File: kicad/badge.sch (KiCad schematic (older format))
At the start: 12 parts, among them SW1 SPST

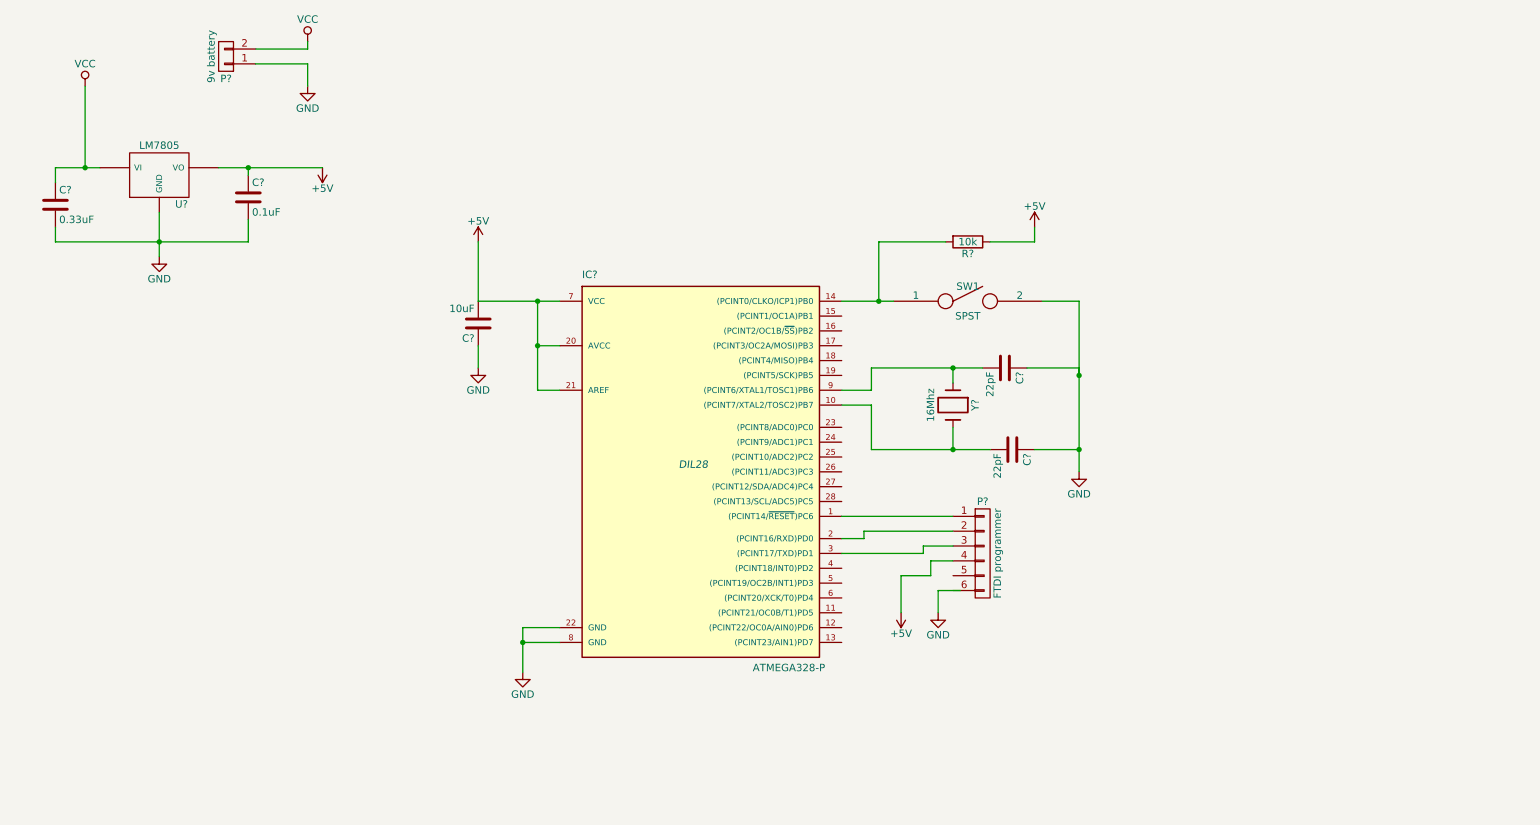
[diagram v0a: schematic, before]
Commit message: use wire labels to organize schematic
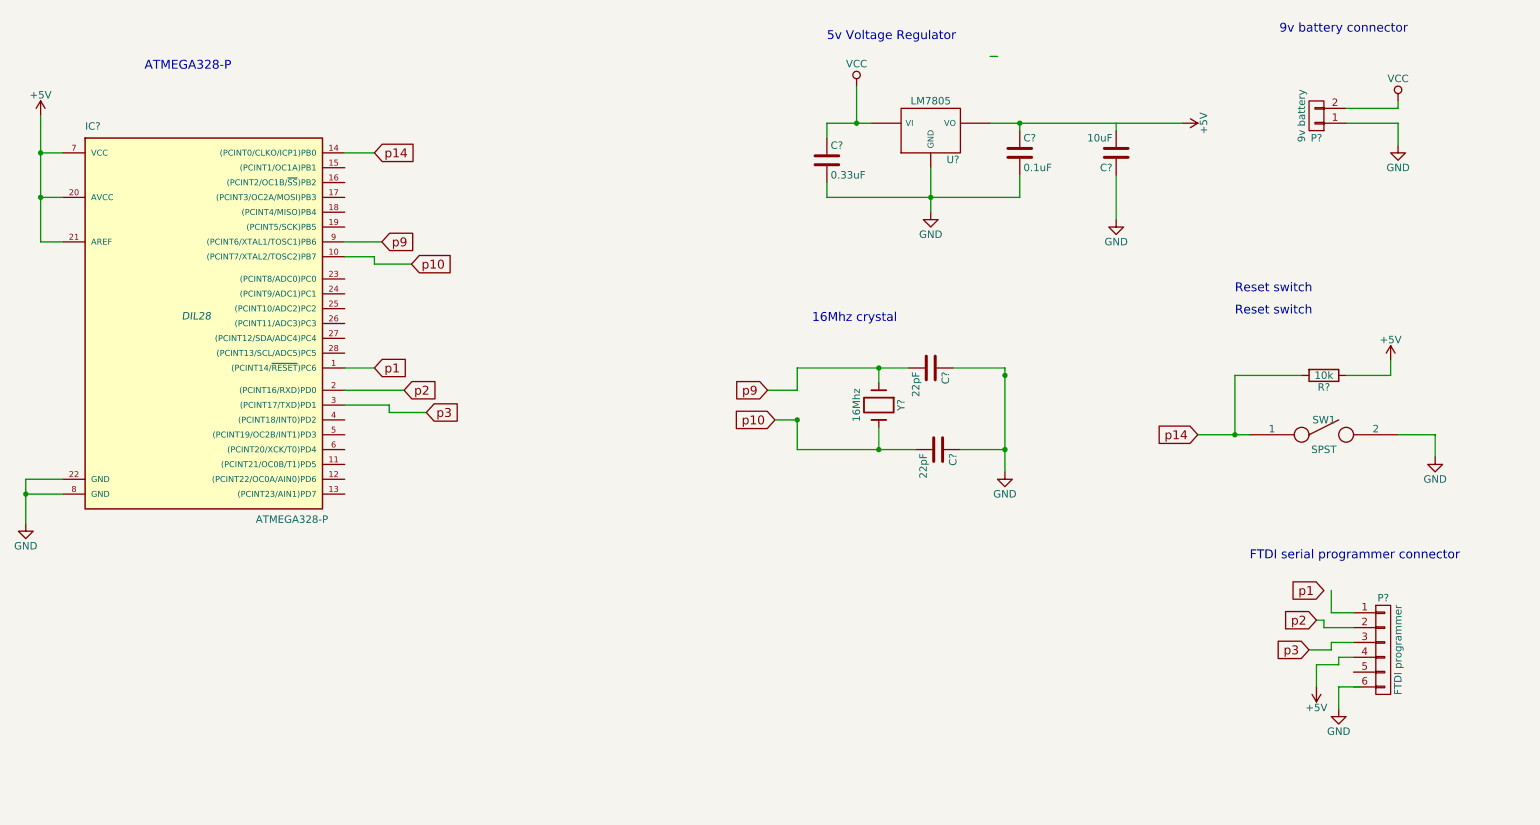
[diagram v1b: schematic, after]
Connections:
- net labels added: p1, p10, p14, p2, p3, p9
- wire segments 53 -> 65
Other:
- note added: "16Mhz crystal"
- note added: "5v Voltage Regulator"
- note added: "9v battery connector"
- note added: "ATMEGA328-P"
- note added: "FTDI serial programmer connector"
- note added: "Reset switch"
- moved on the sheet: C?, IC?, P?, R?, SW1, U?, Y?

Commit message: display connector
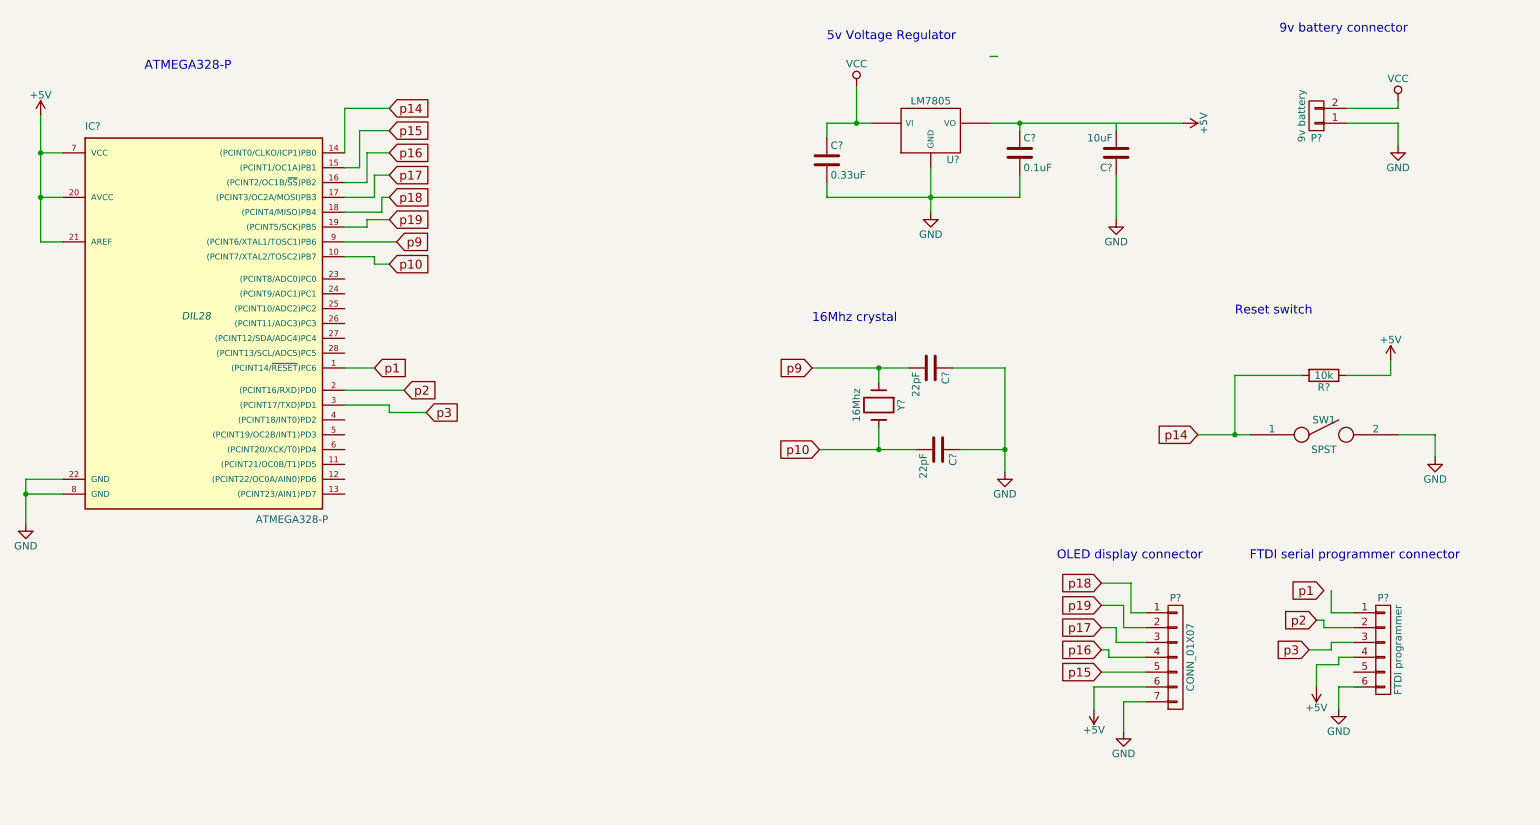
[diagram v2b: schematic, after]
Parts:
- added P?: CONN_01X07, symbol CONN_01X07
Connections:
- net labels added: p15, p16, p17, p18, p19
- wire segments 65 -> 94
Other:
- note added: "OLED display connector"
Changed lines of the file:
@@
 	1    0    0    -1
 $EndComp
-Text GLabel 3450 1650 2    60   Input ~ 0
+Text GLabel 3550 1350 2    60   Input ~ 0
 p14
 Text GLabel 9000 3550 0    60   Input ~ 0
 p14
-Text GLabel 3500 2250 2    60   Input ~ 0
+Text GLabel 3600 2250 2    60   Input ~ 0
 p9
-Text GLabel 3700 2400 2    60   Input ~ 0
+Text GLabel 3550 2400 2    60   Input ~ 0
 p10
-Text GLabel 6100 3250 0    60   Input ~ 0
+Text GLabel 6400 3100 0    60   Input ~ 0
 p9
-Text GLabel 6150 3450 0    60   Input ~ 0
+Text GLabel 6450 3650 0    60   Input ~ 0
 p10
 Text GLabel 3450 3100 2    60   Input ~ 0
@@
 $EndComp
 Wire Wire Line
-	6300 3100 7050 3100
-Wire Wire Line
 	6850 3200 6850 3100
 Wire Wire Line
 	6850 3500 6850 3650
-Wire Wire Line
-	6300 3650 7100 3650
 Wire Wire Line
 	7350 3100 7700 3100
@@
 	6700 1200 6700 1450
 Connection ~ 6700 1450
-Wire Wire Line
-	6100 3250 6300 3250
-Wire Wire Line
-	6300 3250 6300 3100
 Connection ~ 6850 3100
 Connection ~ 6850 3650
@@
 Wire Wire Line
 	10350 3550 10600 3550
-Connection ~ 7700 3150
 Wire Wire Line
 	10000 1350 10350 1350
@@
 	10600 3550 10600 3700
 Wire Wire Line
-	3250 1650 3450 1650
-Wire Wire Line
-	3250 2250 3500 2250
+	3250 2250 3600 2250
 Wire Wire Line
 	3250 2350 3450 2350
@@
 	3450 2350 3450 2400
 Wire Wire Line
-	3450 2400 3700 2400
-Wire Wire Line
-	6150 3450 6300 3450
-Connection ~ 6300 3450
-Wire Wire Line
-	6300 3450 6300 3650
-Wire Wire Line
 	3250 3100 3450 3100
 Wire Wire Line
@@
 	1200 2250 1350 2250
 Wire Wire Line
-	1350 1950 1200 1950
+	1200 1950 1350 1950
 Connection ~ 1200 1650
 Connection ~ 1200 1950
@@
 Text Notes 6400 2800 0    60   ~ 0
 16Mhz crystal
-Text Notes 9250 2600 0    60   ~ 0
-Reset switch
 Text Notes 9350 4400 0    60   ~ 0
 FTDI serial programmer connector
@@
 Text Notes 9250 2750 0    60   ~ 0
 Reset switch
+Wire Wire Line
+	6400 3100 7050 3100
+Wire Wire Line
+	6450 3650 7100 3650
+$Comp
+L GND #PWR?
+U 1 1 58E46BE0
+P 8500 5550
+F 0 "#PWR?" H 8500 5300 50  0001 C CNN
+F 1 "GND" H 8500 5400 50  0000 C CNN
+F 2 "" H 8500 5550 50  0000 C CNN
+F 3 "" H 8500 5550 50  0000 C CNN
+	1    8500 5550
+	1    0    0    -1
+$EndComp
+Wire Wire Line
+	8650 5350 8500 5350
+Wire Wire Line
+	8500 5350 8500 5550
+$Comp
+L +5V #PWR?
+U 1 1 58E46C64
+P 8300 5400
+F 0 "#PWR?" H 8300 5250 50  0001 C CNN
+F 1 "+5V" H 8300 5540 50  0000 C CNN
+F 2 "" H 8300 5400 50  0000 C CNN
+F 3 "" H 8300 5400 50  0000 C CNN
+	1    8300 5400
+	-1   0    0    1
+$EndComp
+Wire Wire Line
+	8650 5250 8300 5250
+Wire Wire Line
+	8300 5250 8300 5400
+Text GLabel 8350 4700 0    60   Input ~ 0
+p19
+Text GLabel 8350 4850 0    60   Input ~ 0
+p17
+Text GLabel 8350 5000 0    60   Input ~ 0
+p16
+Text GLabel 8350 5150 0    60   Input ~ 0
+p15
+Wire Wire Line
+	8350 5150 8650 5150
+Wire Wire Line
+	8350 5000 8400 5000
+Wire Wire Line
+	8400 5000 8400 5050
+Wire Wire Line
+	8400 5050 8650 5050
+Wire Wire Line
+	8350 4850 8450 4850
+Wire Wire Line
+	8450 4850 8450 4950
+Wire Wire Line
+	8450 4950 8650 4950
+Wire Wire Line
+	8350 4700 8500 4700
+Wire Wire Line
+	8500 4700 8500 4850
+Wire Wire Line
+	8500 4850 8650 4850
+$Comp
+L CONN_01X07 P?
+U 1 1 58E46FAC
+P 8850 5050
+F 0 "P?" H 8850 5450 50  0000 C CNN
+F 1 "CONN_01X07" V 8950 5050 50  0000 C CNN
+F 2 "" H 8850 5050 50  0000 C CNN
+F 3 "" H 8850 5050 50  0000 C CNN
+	1    8850 5050
+	1    0    0    -1
+$EndComp
+Text GLabel 8350 4550 0    60   Input ~ 0
+p18
+Wire Wire Line
+	8350 4550 8550 4550
+Wire Wire Line
+	8550 4550 8550 4750
+Wire Wire Line
+	8550 4750 8650 4750
+Text Notes 8050 4400 0    60   ~ 0
+OLED display connector
+Text GLabel 3550 1500 2    60   Input ~ 0
+p15
+Text GLabel 3550 1650 2    60   Input ~ 0
+p16
+Text GLabel 3550 1800 2    60   Input ~ 0
+p17
+Text GLabel 3550 1950 2    60   Input ~ 0
+p18
+Text GLabel 3550 2100 2    60   Input ~ 0
+p19
+Wire Wire Line
+	3250 2150 3400 2150
+Wire Wire Line
+	3400 2150 3400 2100
+Wire Wire Line
+	3400 2100 3550 2100
+Wire Wire Line
+	3250 2050 3500 2050
+Wire Wire Line
+	3500 2050 3500 1950
+Wire Wire Line
+	3500 1950 3550 1950
+Wire Wire Line
+	3250 1950 3450 1950
+Wire Wire Line
+	3450 1950 3450 1800
+Wire Wire Line
+	3450 1800 3550 1800
+Wire Wire Line
+	3250 1850 3400 1850
+Wire Wire Line
+	3400 1850 3400 1650
+Wire Wire Line
+	3400 1650 3550 1650
+Wire Wire Line
+	3250 1750 3350 1750
+Wire Wire Line
+	3350 1750 3350 1500
+Wire Wire Line
+	3350 1500 3550 1500
+Wire Wire Line
+	3250 1650 3250 1350
+Wire Wire Line
+	3250 1350 3550 1350
+Wire Wire Line
+	3450 2400 3550 2400
 $EndSCHEMATC

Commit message: netlist
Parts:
- gave numbers to parts that had none: 12
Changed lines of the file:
@@
 $EndDescr
 $Comp
-L R R?
+L R R1
 U 1 1 58E15AC1
 P 9850 3150
-F 0 "R?" V 9930 3150 50  0000 C CNN
+F 0 "R1" V 9930 3150 50  0000 C CNN
 F 1 "10k" V 9850 3150 50  0000 C CNN
 F 2 "" V 9780 3150 50  0000 C CNN
@@
 $EndComp
 $Comp
-L C C?
+L C C2
 U 1 1 58E15B8A
 P 7200 3100
-F 0 "C?" H 7225 3200 50  0000 L CNN
+F 0 "C2" H 7225 3200 50  0000 L CNN
 F 1 "22pF" H 7225 3000 50  0000 L CNN
 F 2 "" H 7238 2950 50  0000 C CNN
@@
 $EndComp
 $Comp
-L GND #PWR04
+L GND #PWR01
 U 1 1 58E16135
 P 7700 3800
-F 0 "#PWR04" H 7700 3550 50  0001 C CNN
+F 0 "#PWR01" H 7700 3550 50  0001 C CNN
 F 1 "GND" H 7700 3650 50  0000 C CNN
 F 2 "" H 7700 3800 50  0000 C CNN
@@
 $EndComp
 $Comp
-L C C?
+L C C5
 U 1 1 58E164D8
 P 8450 1650
-F 0 "C?" H 8475 1750 50  0000 L CNN
+F 0 "C5" H 8475 1750 50  0000 L CNN
 F 1 "10uF" H 8475 1550 50  0000 L CNN
 F 2 "" H 8488 1500 50  0000 C CNN
@@
 $EndComp
 $Comp
-L GND #PWR05
+L GND #PWR02
 U 1 1 58E16557
 P 8450 2100
-F 0 "#PWR05" H 8450 1850 50  0001 C CNN
+F 0 "#PWR02" H 8450 1850 50  0001 C CNN
 F 1 "GND" H 8450 1950 50  0000 C CNN
 F 2 "" H 8450 2100 50  0000 C CNN
@@
 $EndComp
 $Comp
-L LM7805 U?
+L LM7805 U1
 U 1 1 58E194B3
 P 7200 1500
-F 0 "U?" H 7350 1304 50  0000 C CNN
+F 0 "U1" H 7350 1304 50  0000 C CNN
 F 1 "LM7805" H 7200 1700 50  0000 C CNN
 F 2 "" H 7200 1500 50  0000 C CNN
@@
 $EndComp
 $Comp
-L GND #PWR?
+L GND #PWR03
 U 1 1 58E194EE
 P 7200 2050
-F 0 "#PWR?" H 7200 1800 50  0001 C CNN
+F 0 "#PWR03" H 7200 1800 50  0001 C CNN
 F 1 "GND" H 7200 1900 50  0000 C CNN
 F 2 "" H 7200 2050 50  0000 C CNN
@@
 $EndComp
 $Comp
-L C C?
+L C C4
 U 1 1 58E19514
 P 7800 1650
-F 0 "C?" H 7825 1750 50  0000 L CNN
+F 0 "C4" H 7825 1750 50  0000 L CNN
 F 1 "0.1uF" H 7825 1550 50  0000 L CNN
 F 2 "" H 7838 1500 50  0000 C CNN
@@
 $EndComp
 $Comp
-L C C?
+L C C1
 U 1 1 58E19563
 P 6500 1700
-F 0 "C?" H 6525 1800 50  0000 L CNN
+F 0 "C1" H 6525 1800 50  0000 L CNN
 F 1 "0.33uF" H 6525 1600 50  0000 L CNN
 F 2 "" H 6538 1550 50  0000 C CNN
@@
 $EndComp
 $Comp
-L +5V #PWR?
+L +5V #PWR04
 U 1 1 58E198B5
 P 10300 3050
-F 0 "#PWR?" H 10300 2900 50  0001 C CNN
+F 0 "#PWR04" H 10300 2900 50  0001 C CNN
 F 1 "+5V" H 10300 3190 50  0000 C CNN
 F 2 "" H 10300 3050 50  0000 C CNN
@@
 $EndComp
 $Comp
-L VCC #PWR?
+L VCC #PWR05
 U 1 1 58E19A0A
 P 6700 1200
-F 0 "#PWR?" H 6700 1050 50  0001 C CNN
+F 0 "#PWR05" H 6700 1050 50  0001 C CNN
 F 1 "VCC" H 6700 1350 50  0000 C CNN
 F 2 "" H 6700 1200 50  0000 C CNN
@@
 $EndComp
 $Comp
-L ATMEGA328-P IC?
+L ATMEGA328-P IC1
 U 1 1 58E19C48
 P 2250 2750
-F 0 "IC?" H 1500 4000 50  0000 L BNN
+F 0 "IC1" H 1500 4000 50  0000 L BNN
 F 1 "ATMEGA328-P" H 2650 1350 50  0000 L BNN
 F 2 "DIL28" H 2250 2750 50  0000 C CIN
@@
 $EndComp
 $Comp
-L CONN_01X02 P?
+L CONN_01X02 P2
 U 1 1 58E1B172
 P 9800 1400
-F 0 "P?" H 9800 1550 50  0000 C CNN
+F 0 "P2" H 9800 1550 50  0000 C CNN
 F 1 "9v battery " V 9900 1400 50  0000 C CNN
 F 2 "" H 9800 1400 50  0000 C CNN
@@
 $EndComp
 $Comp
-L VCC #PWR?
+L VCC #PWR06
 U 1 1 58E1B2A6
 P 10350 1300
-F 0 "#PWR?" H 10350 1150 50  0001 C CNN
+F 0 "#PWR06" H 10350 1150 50  0001 C CNN
 F 1 "VCC" H 10350 1450 50  0000 C CNN
 F 2 "" H 10350 1300 50  0000 C CNN
@@
 $EndComp
 $Comp
-L GND #PWR?
+L GND #PWR07
 U 1 1 58E1B2D2
 P 10350 1600
-F 0 "#PWR?" H 10350 1350 50  0001 C CNN
+F 0 "#PWR07" H 10350 1350 50  0001 C CNN
 F 1 "GND" H 10350 1450 50  0000 C CNN
 F 2 "" H 10350 1600 50  0000 C CNN
@@
 $EndComp
 $Comp
-L CONN_01X06 P?
+L CONN_01X06 P3
 U 1 1 58E1B8C9
 P 10250 5000
-F 0 "P?" H 10250 5350 50  0000 C CNN
+F 0 "P3" H 10250 5350 50  0000 C CNN
 F 1 "FTDI programmer" V 10350 5000 50  0000 C CNN
 F 2 "" H 10250 5000 50  0000 C CNN
@@
 $EndComp
 $Comp
-L GND #PWR?
+L GND #PWR08
 U 1 1 58E1B9A0
 P 9950 5400
-F 0 "#PWR?" H 9950 5150 50  0001 C CNN
+F 0 "#PWR08" H 9950 5150 50  0001 C CNN
 F 1 "GND" H 9950 5250 50  0000 C CNN
 F 2 "" H 9950 5400 50  0000 C CNN
@@
 $EndComp
 $Comp
-L +5V #PWR?
+L +5V #PWR09
 U 1 1 58E1BF97
 P 9800 5250
-F 0 "#PWR?" H 9800 5100 50  0001 C CNN
+F 0 "#PWR09" H 9800 5100 50  0001 C CNN
 F 1 "+5V" H 9800 5390 50  0000 C CNN
 F 2 "" H 9800 5250 50  0000 C CNN
@@
 $EndComp
 $Comp
-L Crystal Y?
+L Crystal Y1
 U 1 1 58E1C7EA
 P 6850 3350
-F 0 "Y?" H 6850 3500 50  0000 C CNN
+F 0 "Y1" H 6850 3500 50  0000 C CNN
 F 1 "16Mhz" H 6850 3200 50  0000 C CNN
 F 2 "" H 6850 3350 50  0000 C CNN
@@
 $EndComp
 $Comp
-L C C?
+L C C3
 U 1 1 58E1C898
 P 7250 3650
-F 0 "C?" H 7275 3750 50  0000 L CNN
+F 0 "C3" H 7275 3750 50  0000 L CNN
 F 1 "22pF" H 7275 3550 50  0000 L CNN
 F 2 "" H 7288 3500 50  0000 C CNN
@@
 $EndComp
 $Comp
-L GND #PWR?
+L GND #PWR010
 U 1 1 58E35C64
 P 10600 3700
-F 0 "#PWR?" H 10600 3450 50  0001 C CNN
+F 0 "#PWR010" H 10600 3450 50  0001 C CNN
 F 1 "GND" H 10600 3550 50  0000 C CNN
 F 2 "" H 10600 3700 50  0000 C CNN
@@
 p1
 $Comp
-L +5V #PWR?
+L +5V #PWR011
 U 1 1 58E36E45
 P 8900 1450
-F 0 "#PWR?" H 8900 1300 50  0001 C CNN
+F 0 "#PWR011" H 8900 1300 50  0001 C CNN
 F 1 "+5V" H 8900 1590 50  0000 C CNN
 F 2 "" H 8900 1450 50  0000 C CNN
@@
 $EndComp
 $Comp
-L GND #PWR01
+L GND #PWR012
 U 1 1 58E15A16
 P 1100 4150
-F 0 "#PWR01" H 1100 3900 50  0001 C CNN
+F 0 "#PWR012" H 1100 3900 50  0001 C CNN
 F 1 "GND" H 1100 4000 50  0000 C CNN
 F 2 "" H 1100 4150 50  0000 C CNN
@@
 	1200 1400 1200 2250
 $Comp
-L +5V #PWR?
+L +5V #PWR013
 U 1 1 58E37469
 P 1200 1400
-F 0 "#PWR?" H 1200 1250 50  0001 C CNN
+F 0 "#PWR013" H 1200 1250 50  0001 C CNN
 F 1 "+5V" H 1200 1540 50  0000 C CNN
 F 2 "" H 1200 1400 50  0000 C CNN
@@
 	6450 3650 7100 3650
 $Comp
-L GND #PWR?
+L GND #PWR014
 U 1 1 58E46BE0
 P 8500 5550
-F 0 "#PWR?" H 8500 5300 50  0001 C CNN
+F 0 "#PWR014" H 8500 5300 50  0001 C CNN
 F 1 "GND" H 8500 5400 50  0000 C CNN
 F 2 "" H 8500 5550 50  0000 C CNN
@@
 	8500 5350 8500 5550
 $Comp
-L +5V #PWR?
+L +5V #PWR015
 U 1 1 58E46C64
 P 8300 5400
-F 0 "#PWR?" H 8300 5250 50  0001 C CNN
+F 0 "#PWR015" H 8300 5250 50  0001 C CNN
 F 1 "+5V" H 8300 5540 50  0000 C CNN
 F 2 "" H 8300 5400 50  0000 C CNN
@@
 	8500 4850 8650 4850
 $Comp
-L CONN_01X07 P?
+L CONN_01X07 P1
 U 1 1 58E46FAC
 P 8850 5050
-F 0 "P?" H 8850 5450 50  0000 C CNN
+F 0 "P1" H 8850 5450 50  0000 C CNN
 F 1 "CONN_01X07" V 8950 5050 50  0000 C CNN
 F 2 "" H 8850 5050 50  0000 C CNN
